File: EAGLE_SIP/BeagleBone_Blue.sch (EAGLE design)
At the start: 209 parts, among them IC1 WL1835MODGBMOCT, J1 USD_CONNECTOR, M1 JST_ZH_2, M2 JST_ZH_2, M3 JST_ZH_2, M4 JST_ZH_2, Q3 MOSFET-N, U1 LOGIC-TXS0102DCTR(MSOP8), U5 24LC_32AT-I/OT, U6 SN74LVC1G07_DCK_5, U8 MTFC4GLDEA, Y1 CM200C-32.768KAZF-UT, Y2 445C33D24M00000

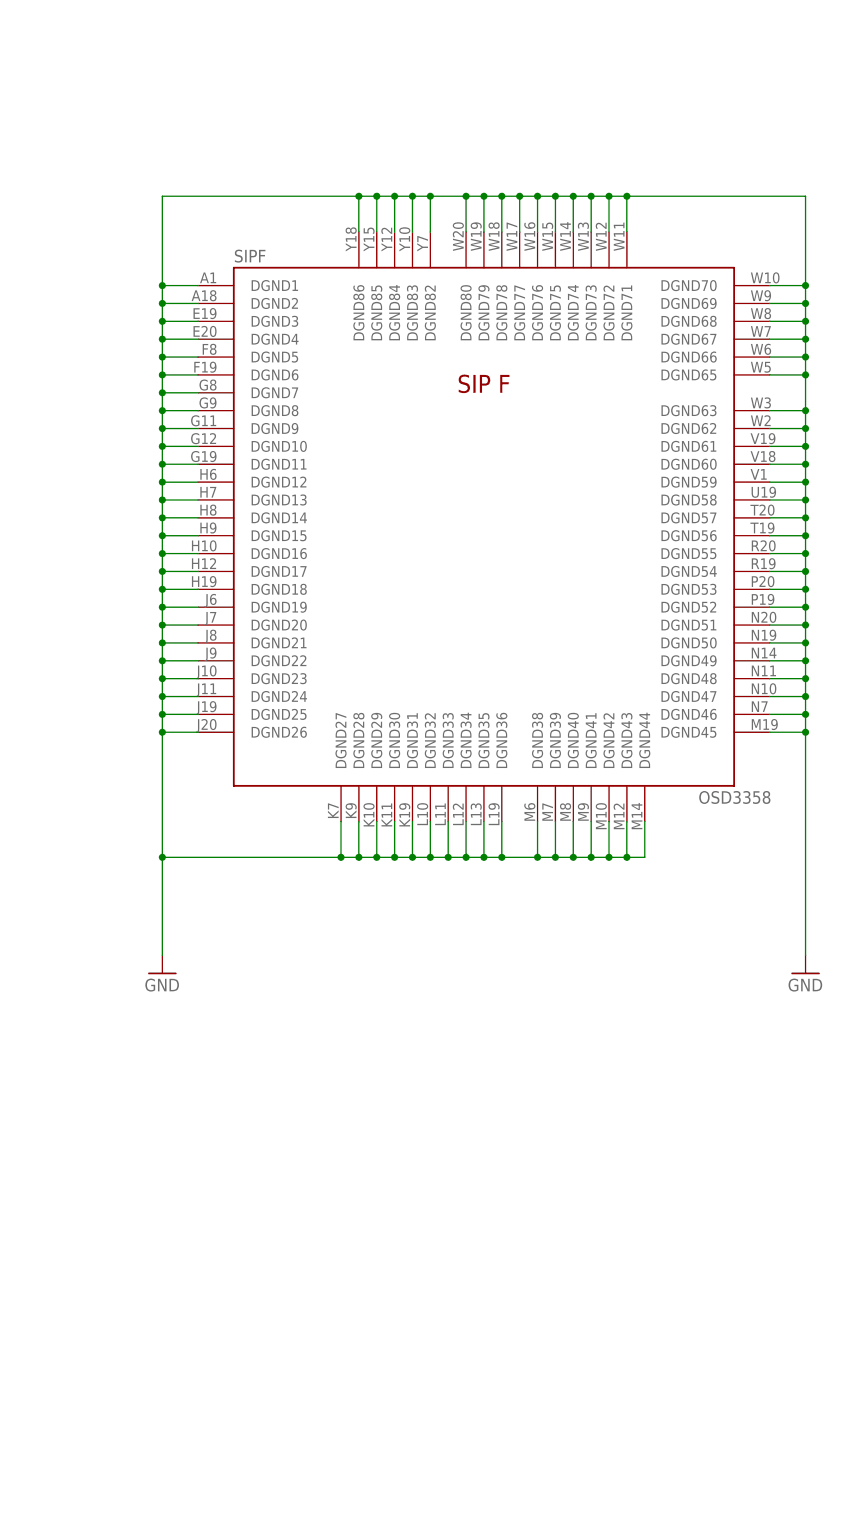
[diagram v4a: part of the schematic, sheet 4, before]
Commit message: Added resistors to clock circuits.
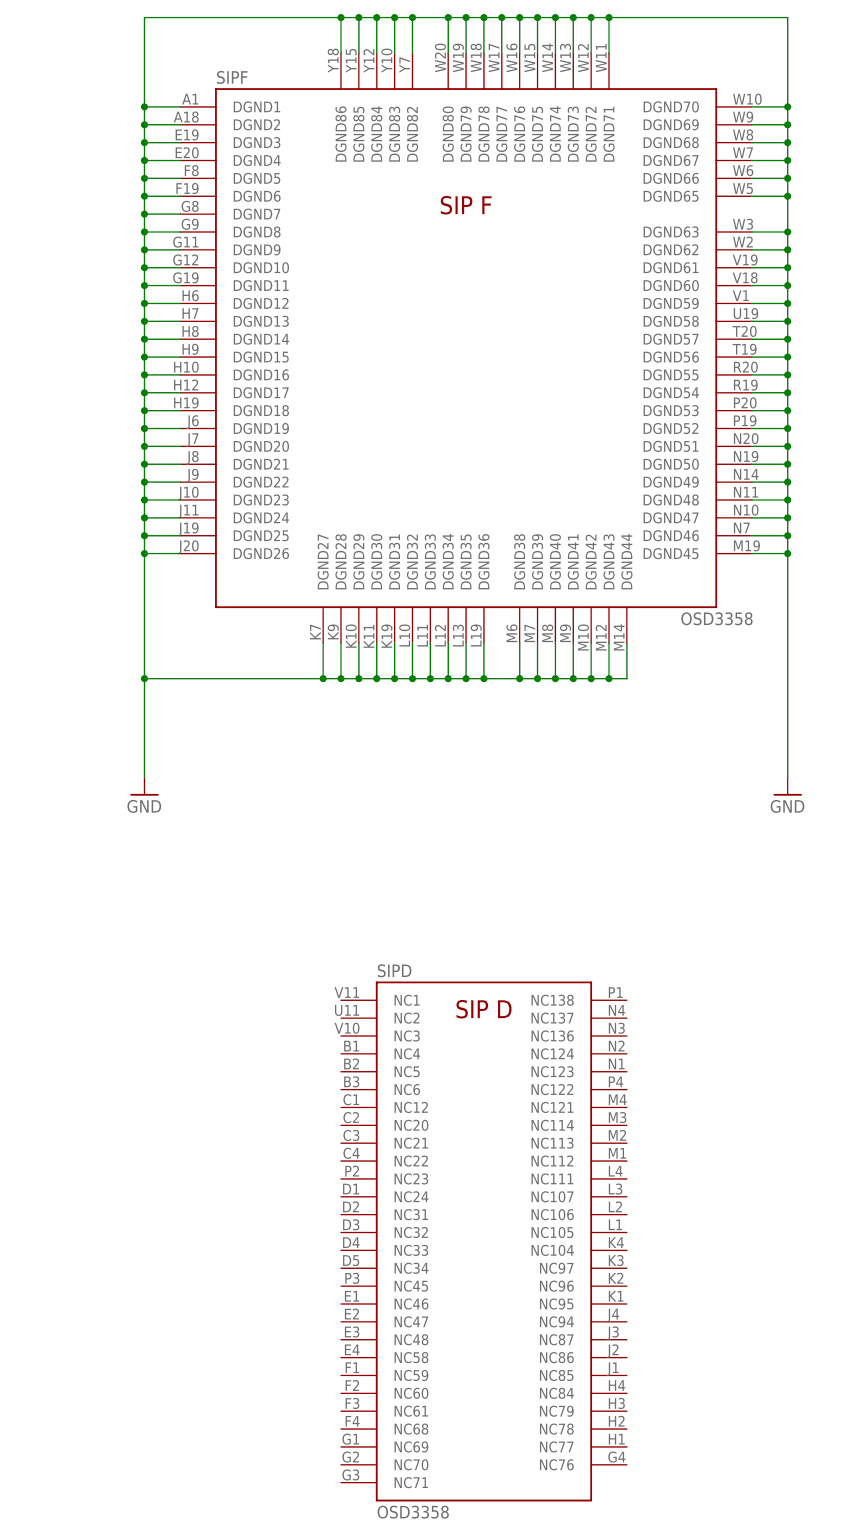
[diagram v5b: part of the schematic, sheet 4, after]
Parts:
- added R18, R20: 1M, Strawson_Eagle_Lib:RESISTOR0402-RES
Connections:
- new net N$86: U5.SDA
- net I2C0_SDA: no longer U5.SDA
- net N$26: now also R20.2
- net N$27: now also R20.1
- net N$32: now also R18.2
- net N$33: now also R18.1
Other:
- moved on the sheet: C29, C30, SIPF

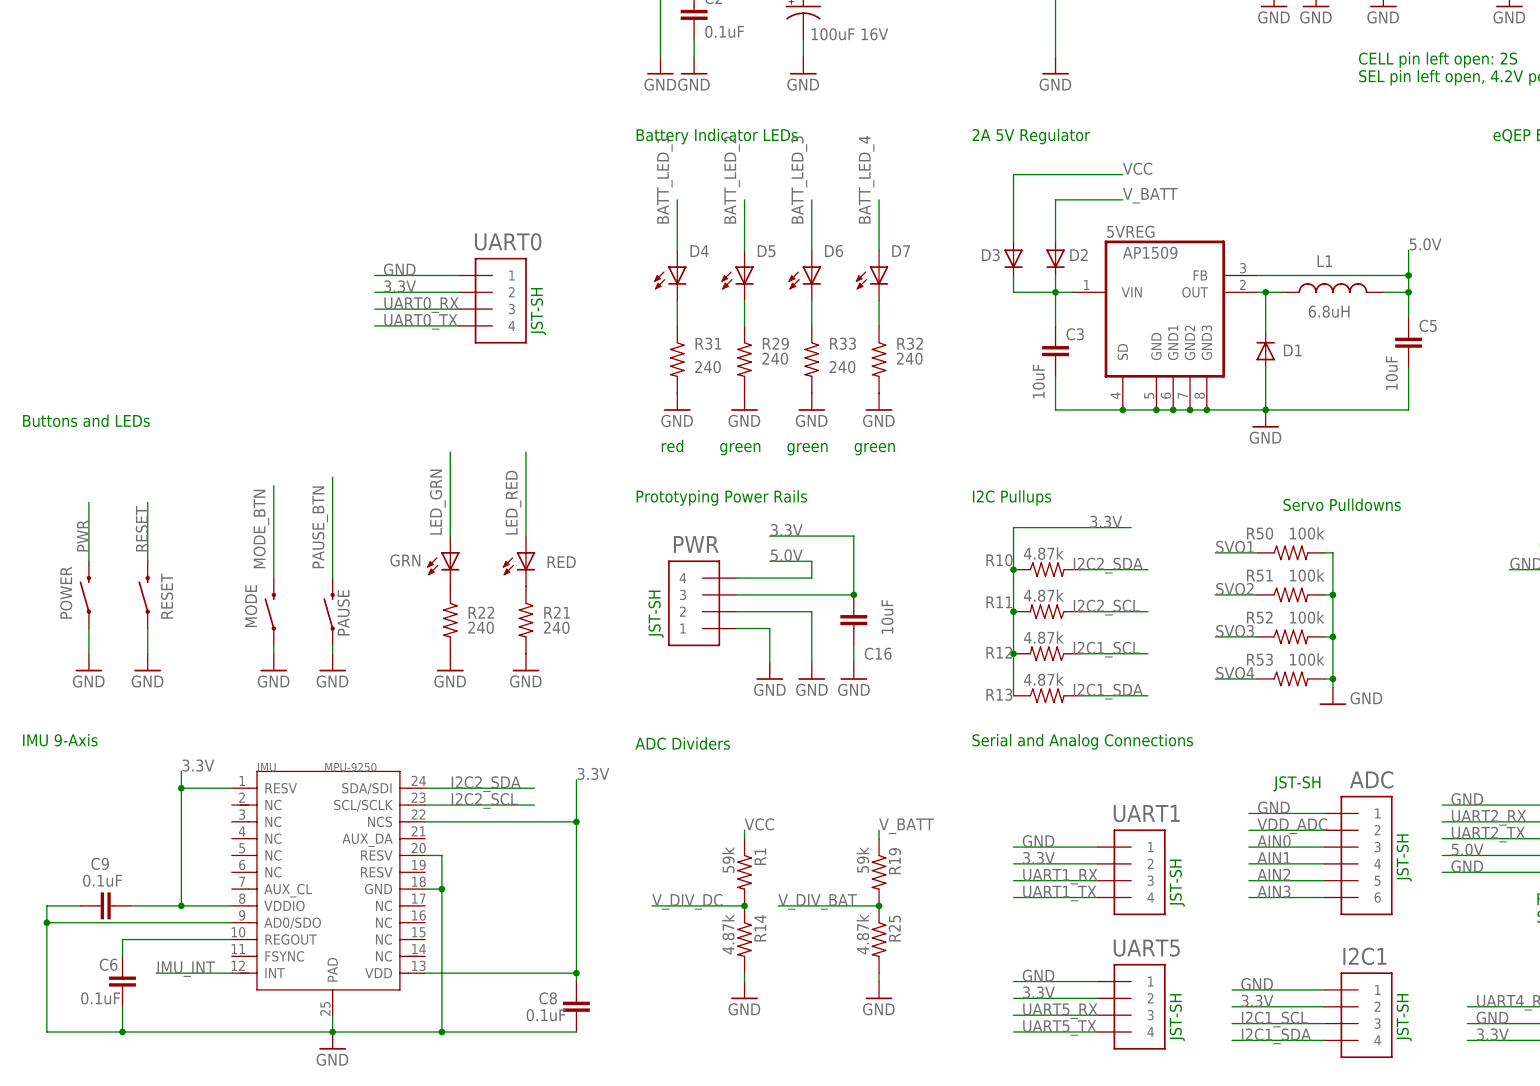
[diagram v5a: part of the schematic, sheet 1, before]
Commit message: Added grove connectors; SD boot pushbutton
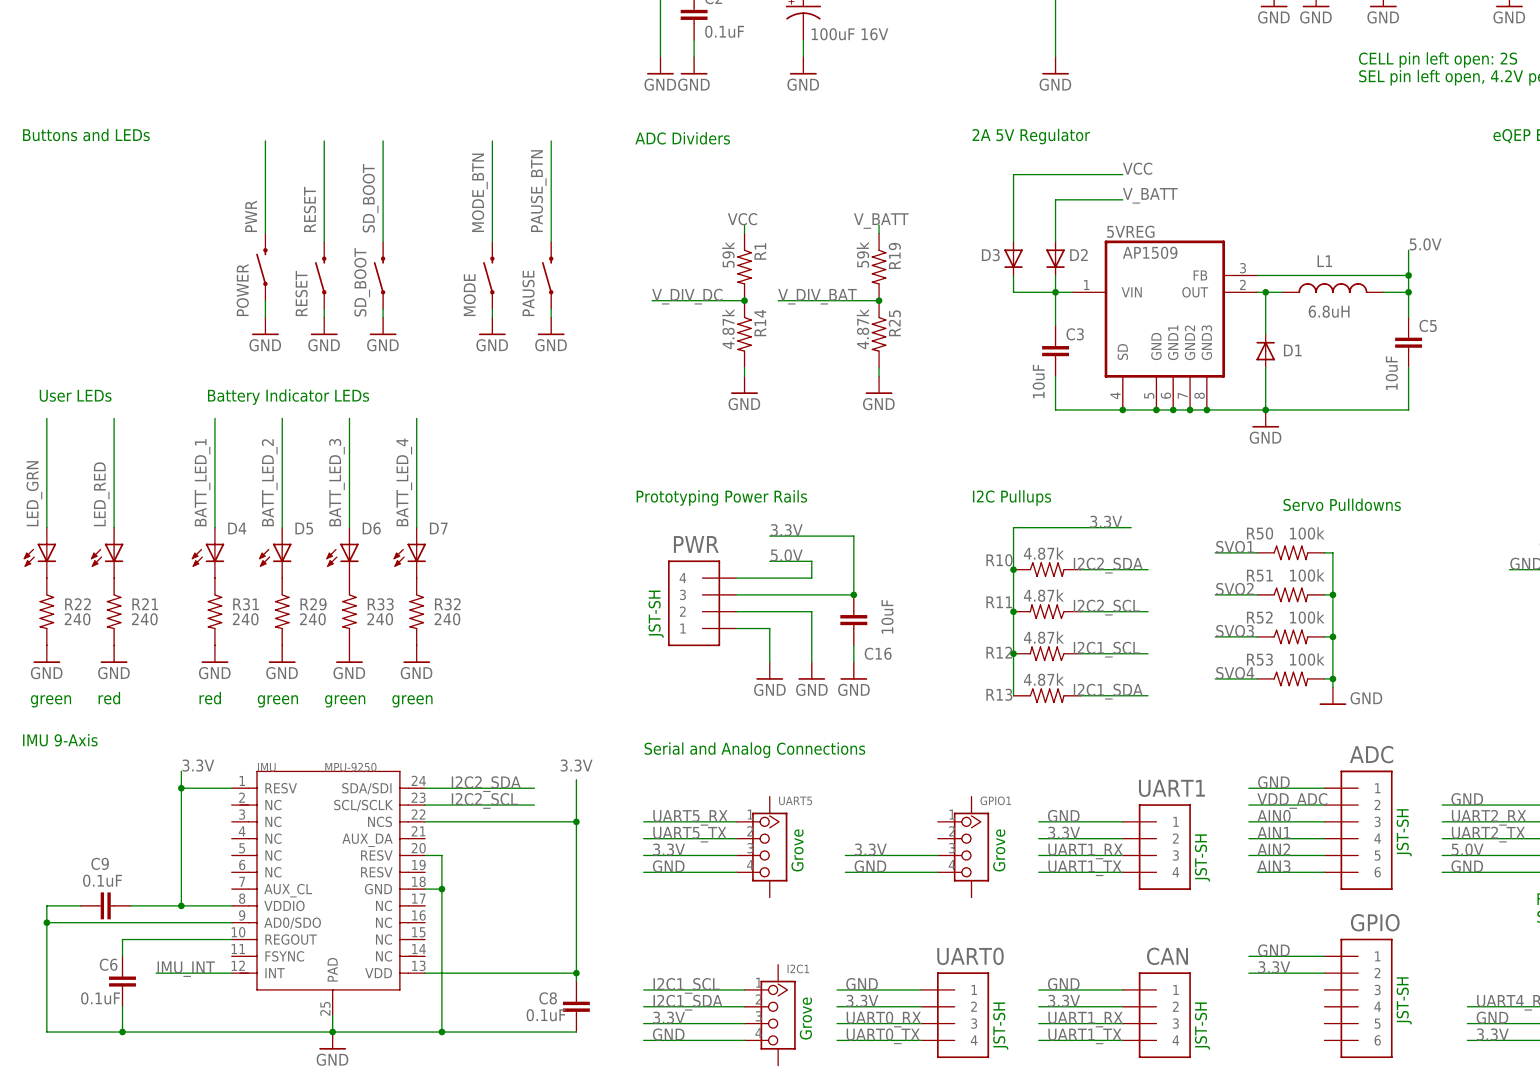
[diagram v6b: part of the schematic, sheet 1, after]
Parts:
- added CAN: JST_SH_4, Strawson_Eagle_Lib:JST_SH_4
- added GPIO: JST_SH_6, Strawson_Eagle_Lib:JST_SH_6
- added GPIO1: (no value), Seeed-Connector -2016:GROVE-CONNECTOR-SMD(4+2P-2.0)
- added SD_BOOT: SWITCH-MOMENTARY-2SMD-1101NE, SparkFun-Electromechanical:SWITCH-MOMENTARY-2SMD-1101NE
- I2C1, UART5: value JST_SH_4 -> (none); device Strawson_Eagle_Lib:JST_SH_4 -> Seeed-Connector -2016:GROVE-CONNECTOR-SMD(4+2P-2.0)
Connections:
- new net SD_BOOT: SD_BOOT.2
- net 3.3V: now also CAN.2, GPIO.2, GPIO1.3, I2C1.3, UART5.3; no longer I2C1.2, UART5.2
- net GND: now also CAN.1, GPIO.1, GPIO1.4, I2C1.4, SD_BOOT.1, UART5.4; no longer I2C1.1, UART5.1
- net I2C1_SCL: now also I2C1.1; no longer I2C1.3
- net I2C1_SDA: now also I2C1.2; no longer I2C1.4
- net UART1_RX: now also CAN.3
- net UART1_TX: now also CAN.4
- net UART5_RX: now also UART5.1; no longer UART5.3
- net UART5_TX: now also UART5.2; no longer UART5.4
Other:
- note added: "Grove"
- note added: "User LEDs"
- moved on the sheet: ADC, D4, D5, D6, D7, MODE, PAUSE, POWER, R1, R14, R19, R21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
